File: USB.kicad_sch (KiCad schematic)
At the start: 0 parts

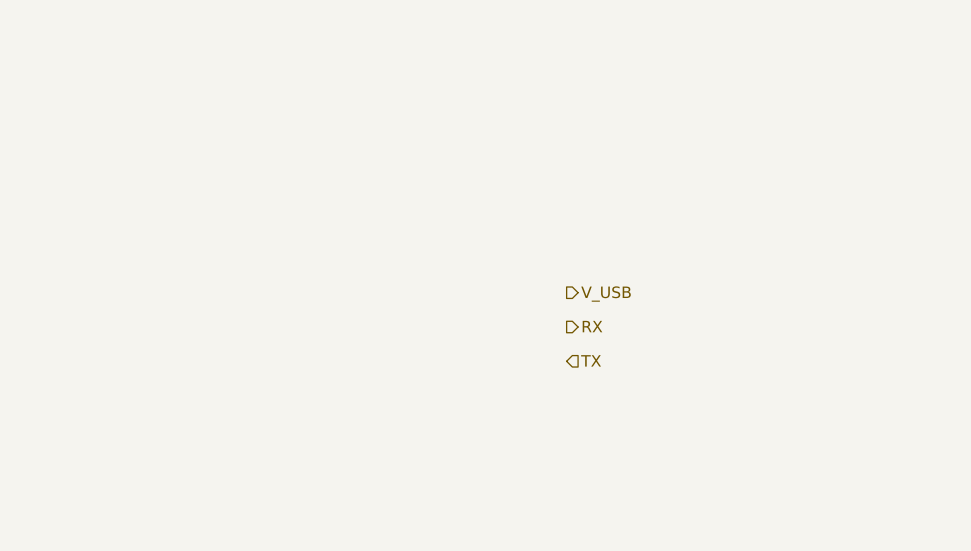
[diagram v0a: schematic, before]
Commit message: added usb serial and mcu
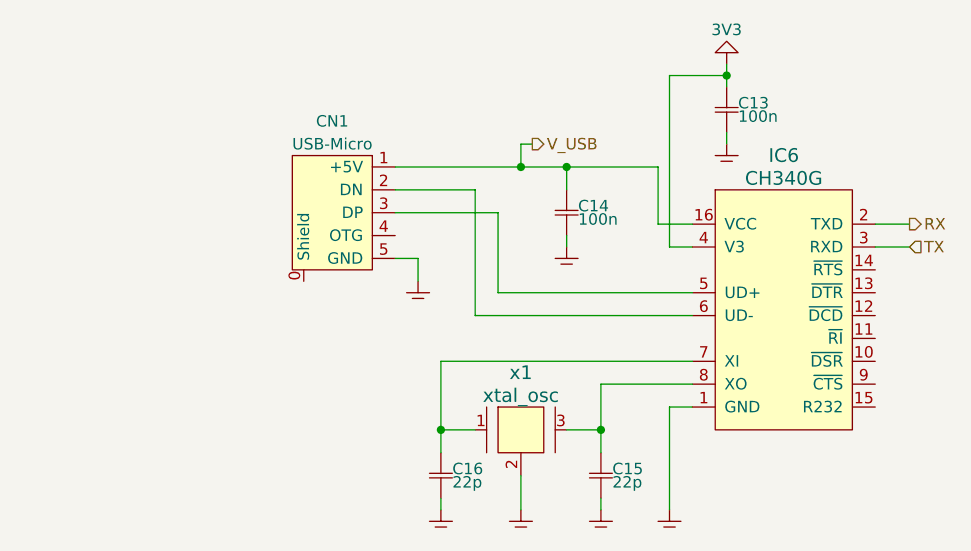
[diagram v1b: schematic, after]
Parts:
- added C13, C14: 100n, SMT:0603, symbol generic:C
- added C15, C16: 22p, SMT:0603, symbol generic:C
- added CN1: USB-Micro, USB:micro_usb, symbol generic:USB-Micro
- added IC6: CH340G, symbol serial:CH340G
- added x1: xtal_osc, symbol oscillators:xtal_osc
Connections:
- net RX: now also IC6.2 (TXD)
- net TX: now also IC6.3 (RXD)
- net V_USB: now also C14.1, CN1.1 (+5V), IC6.16 (VCC)
- new net: CN1.3 (DP), IC6.5 (UD+)
- new net: CN1.2 (DN), IC6.6 (UD-)
- new net: C16.1, IC6.7 (XI), x1.1
- new net: C15.1, IC6.8 (XO), x1.3
- new net GND: C13.1, C13.2, C14.2, C15.2, C16.2, CN1.5 (GND), IC6.1 (GND), IC6.4 (V3), x1.2, x1.4

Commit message: cleaned up layout, added 3V3 regulator, changed NTC to connect to gnd instead of 3V3, added README
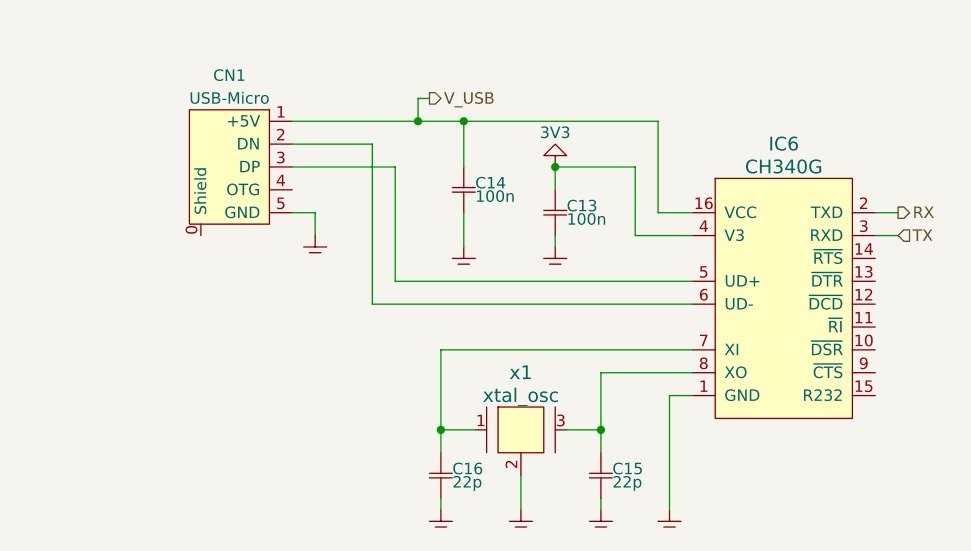
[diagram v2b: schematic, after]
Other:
- moved on the sheet: C13, C14, CN1, IC6

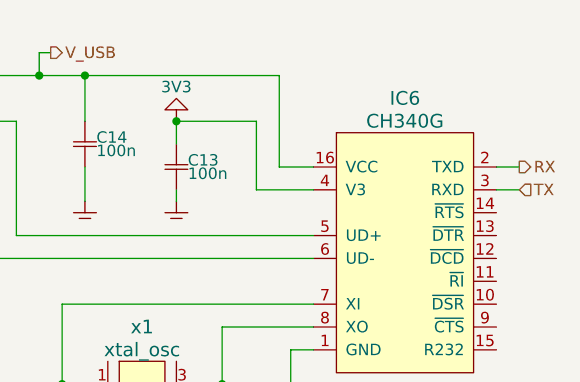
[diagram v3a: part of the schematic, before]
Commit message: started layout, updated readme, annotated power symbols...
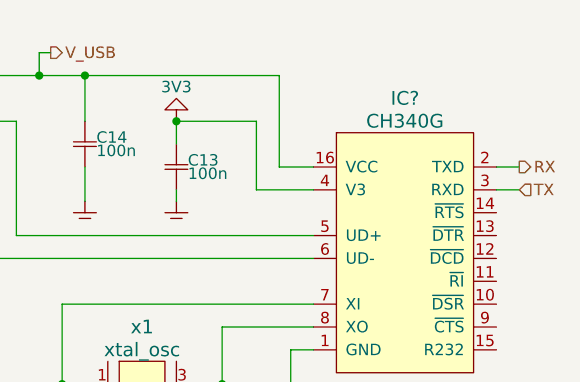
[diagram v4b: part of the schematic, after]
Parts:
- IC?: renamed from IC6; footprint (none) -> SOP:SOP-16
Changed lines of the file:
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@@
   (symbol (lib_id "generic:GND") (at 138.43 121.92 0) (unit 1)
     (in_bom yes) (on_board yes) (dnp no) (fields_autoplaced)
-    (property "Reference" "#GND?" (at 142.24 120.65 0)
+    (property "Reference" "#GND0120" (at 142.24 120.65 0)
       (effects (font (size 1.27 1.27)) hide)
     )
@@
       (project "hikari"
         (path "/020af8ab-593e-45b9-b2cd-8db025796961/bb941b2b-0b73-4110-b4b0-cdc102f480d3"
-          (reference "#GND?") (unit 1)
+          (reference "#GND0120") (unit 1)
         )
       )
@@
   (symbol (lib_id "serial:CH340G") (at 167.64 99.06 0) (unit 1)
     (in_bom yes) (on_board yes) (dnp no) (fields_autoplaced)
-    (property "Reference" "IC6" (at 167.64 81.28 0)
+    (property "Reference" "IC?" (at 167.64 81.28 0)
       (effects (font (size 1.524 1.524)))
     )
@@
       (effects (font (size 1.524 1.524)))
     )
-    (property "Footprint" "" (at 167.64 99.06 0)
-      (effects (font (size 1.524 1.524)))
+    (property "Footprint" "SOP:SOP-16" (at 167.64 99.06 0)
+      (effects (font (size 1.524 1.524)) hide)
     )
     (property "Datasheet" "" (at 167.64 99.06 0)
@@
       (project "hikari"
         (path "/020af8ab-593e-45b9-b2cd-8db025796961/bb941b2b-0b73-4110-b4b0-cdc102f480d3"
-          (reference "IC6") (unit 1)
+          (reference "IC?") (unit 1)
         )
       )
@@
   (symbol (lib_id "generic:GND") (at 129.54 121.92 0) (unit 1)
     (in_bom yes) (on_board yes) (dnp no) (fields_autoplaced)
-    (property "Reference" "#GND?" (at 133.35 120.65 0)
+    (property "Reference" "#GND0121" (at 133.35 120.65 0)
       (effects (font (size 1.27 1.27)) hide)
     )
@@
       (project "hikari"
         (path "/020af8ab-593e-45b9-b2cd-8db025796961/bb941b2b-0b73-4110-b4b0-cdc102f480d3"
-          (reference "#GND?") (unit 1)
+          (reference "#GND0121") (unit 1)
         )
       )
@@
   (symbol (lib_id "generic:GND") (at 115.57 91.44 0) (unit 1)
     (in_bom yes) (on_board yes) (dnp no) (fields_autoplaced)
-    (property "Reference" "#GND?" (at 119.38 90.17 0)
+    (property "Reference" "#GND0124" (at 119.38 90.17 0)
       (effects (font (size 1.27 1.27)) hide)
     )
@@
       (project "hikari"
         (path "/020af8ab-593e-45b9-b2cd-8db025796961/bb941b2b-0b73-4110-b4b0-cdc102f480d3"
-          (reference "#GND?") (unit 1)
+          (reference "#GND0124") (unit 1)
         )
       )
@@
   (symbol (lib_id "generic:GND") (at 154.94 121.92 0) (unit 1)
     (in_bom yes) (on_board yes) (dnp no) (fields_autoplaced)
-    (property "Reference" "#GND?" (at 158.75 120.65 0)
+    (property "Reference" "#GND0119" (at 158.75 120.65 0)
       (effects (font (size 1.27 1.27)) hide)
     )
@@
       (project "hikari"
         (path "/020af8ab-593e-45b9-b2cd-8db025796961/bb941b2b-0b73-4110-b4b0-cdc102f480d3"
-          (reference "#GND?") (unit 1)
+          (reference "#GND0119") (unit 1)
         )
       )
@@
   (symbol (lib_id "generic:GND") (at 132.08 92.71 0) (unit 1)
     (in_bom yes) (on_board yes) (dnp no) (fields_autoplaced)
-    (property "Reference" "#GND?" (at 135.89 91.44 0)
+    (property "Reference" "#GND0123" (at 135.89 91.44 0)
       (effects (font (size 1.27 1.27)) hide)
     )
@@
       (project "hikari"
         (path "/020af8ab-593e-45b9-b2cd-8db025796961/bb941b2b-0b73-4110-b4b0-cdc102f480d3"
-          (reference "#GND?") (unit 1)
+          (reference "#GND0123") (unit 1)
         )
       )
@@
   (symbol (lib_id "generic:GND") (at 142.24 92.71 0) (unit 1)
     (in_bom yes) (on_board yes) (dnp no) (fields_autoplaced)
-    (property "Reference" "#GND?" (at 146.05 91.44 0)
+    (property "Reference" "#GND0122" (at 146.05 91.44 0)
       (effects (font (size 1.27 1.27)) hide)
     )
@@
       (project "hikari"
         (path "/020af8ab-593e-45b9-b2cd-8db025796961/bb941b2b-0b73-4110-b4b0-cdc102f480d3"
-          (reference "#GND?") (unit 1)
+          (reference "#GND0122") (unit 1)
         )
       )
@@
   (symbol (lib_id "generic:GND") (at 147.32 121.92 0) (unit 1)
     (in_bom yes) (on_board yes) (dnp no) (fields_autoplaced)
-    (property "Reference" "#GND?" (at 151.13 120.65 0)
+    (property "Reference" "#GND0118" (at 151.13 120.65 0)
       (effects (font (size 1.27 1.27)) hide)
     )
@@
       (project "hikari"
         (path "/020af8ab-593e-45b9-b2cd-8db025796961/bb941b2b-0b73-4110-b4b0-cdc102f480d3"
-          (reference "#GND?") (unit 1)
+          (reference "#GND0118") (unit 1)
         )
       )
@@
   (symbol (lib_id "generic:3V3") (at 142.24 83.82 0) (unit 1)
     (in_bom yes) (on_board yes) (dnp no)
-    (property "Reference" "#3V?" (at 146.05 82.55 0)
+    (property "Reference" "#3V0101" (at 146.05 82.55 0)
       (effects (font (size 1.27 1.27)) hide)
     )
@@
       (project "hikari"
         (path "/020af8ab-593e-45b9-b2cd-8db025796961/bb941b2b-0b73-4110-b4b0-cdc102f480d3"
-          (reference "#3V?") (unit 1)
-        )
-      )
+          (reference "#3V0101") (unit 1)
+        )
+      )

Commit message: worked layout, fixed 3V3 being GND net
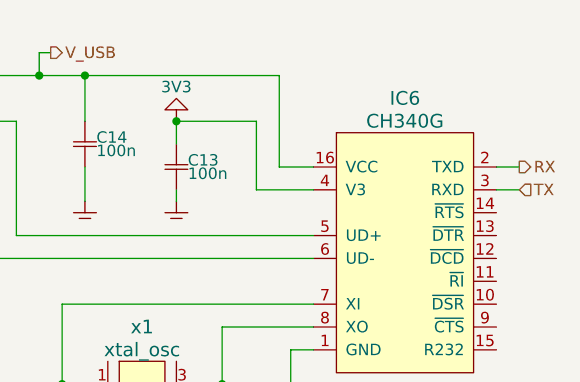
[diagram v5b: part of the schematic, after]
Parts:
- gave numbers to parts that had none: 1
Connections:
- net GND: no longer C13.1, IC6.4 (V3)
- new net 3V3: C13.1, IC6.4 (V3)
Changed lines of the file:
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@@
   (symbol (lib_id "serial:CH340G") (at 167.64 99.06 0) (unit 1)
     (in_bom yes) (on_board yes) (dnp no) (fields_autoplaced)
-    (property "Reference" "IC?" (at 167.64 81.28 0)
+    (property "Reference" "IC6" (at 167.64 81.28 0)
       (effects (font (size 1.524 1.524)))
     )
@@
       (project "hikari"
         (path "/020af8ab-593e-45b9-b2cd-8db025796961/bb941b2b-0b73-4110-b4b0-cdc102f480d3"
-          (reference "IC?") (unit 1)
+          (reference "IC6") (unit 1)
         )
       )

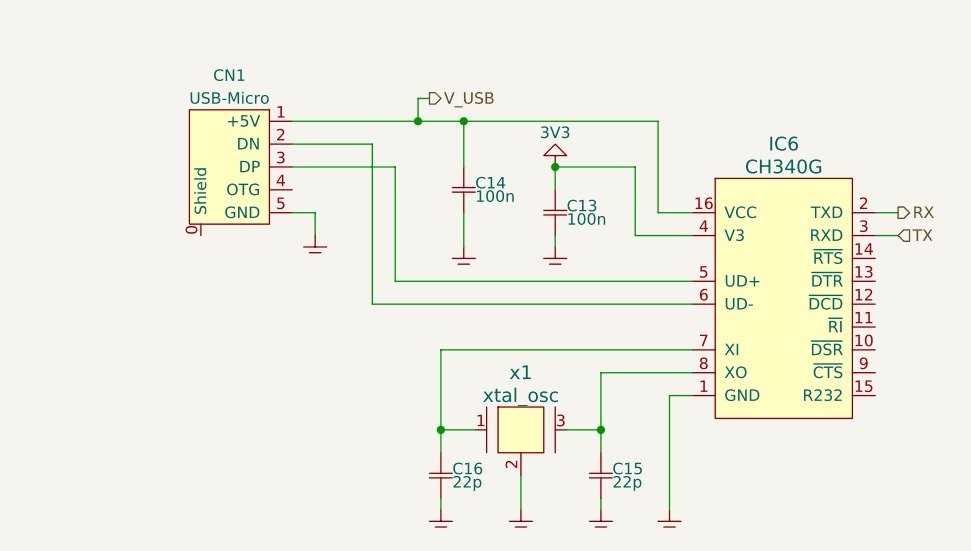
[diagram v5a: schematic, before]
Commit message: added type-c connector
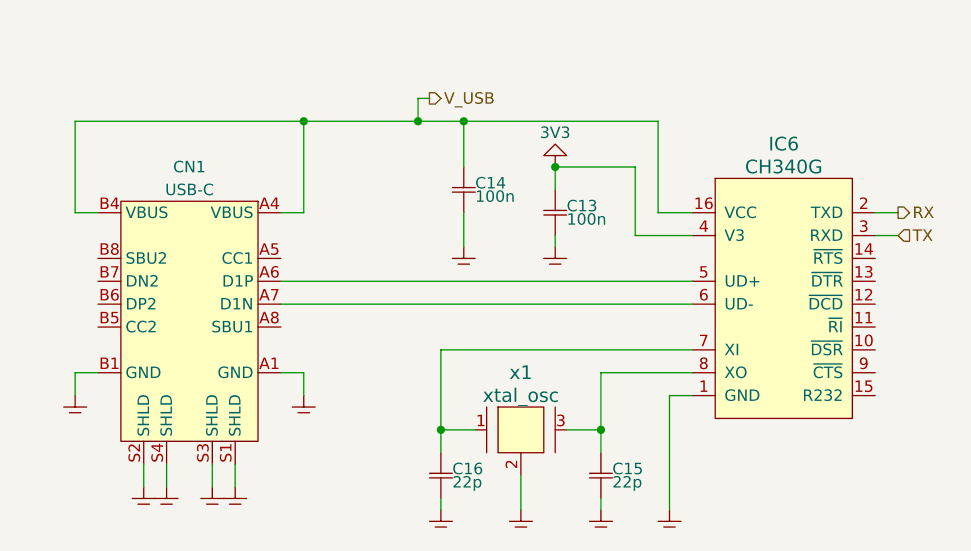
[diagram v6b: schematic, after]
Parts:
- CN1: value USB-Micro -> USB-C; footprint USB:micro_usb -> USB:USB4105-GF-A; symbol generic:USB-Micro -> connectors:USB4105-GF-A; Digi-Key (none) -> 2073-USB4105-GF-ACT-ND; MPN (none) -> USB4105-GF-A
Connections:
- net GND: now also CN1.A1 (GND), CN1.B1 (GND), CN1.S1 (SHLD), CN1.S2 (SHLD), CN1.S3 (SHLD), CN1.S4 (SHLD); no longer CN1.5 (GND)
- net V_USB: now also CN1.A4 (VBUS), CN1.B4 (VBUS); no longer CN1.1 (+5V)
- net at IC6.5 (UD+): now also CN1.A6 (D1P); no longer CN1.3 (DP)
- net at IC6.6 (UD-): now also CN1.A7 (D1N); no longer CN1.2 (DN)
